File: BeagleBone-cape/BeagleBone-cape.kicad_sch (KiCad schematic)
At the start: 92 parts, among them IC2 TCAN3413DDFR, IC3 BMP390, IC4 BMM350, J1 Servo 0, J10 MotorR, J11 CAN, J12 24V, J13 MAVLink, J2 Servo 1, J3 Servo 2, J4 Servo 3, J5 LEDL, J6 LEDR, J7 MAG_I2C_TP, J8 Air Speed Sensor, J9 MotorL, P8 BeagleBone_Black_Header, P9 BeagleBone_Black_Header, Q2 Q_NMOS_GSD, SW1 SW_DIP_x02, U1 CAT24C256, U2 BHI360, U3 DS1307ZN+, Y1 32.768kHz

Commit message: Add i2c logic level translator
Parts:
- added C19: 100n, Capacitor_SMD:C_0603_1608Metric_Pad1.08x0.95mm_HandSolder, symbol Device:C_Small
- added C20, C21: 1u, Capacitor_SMD:C_0603_1608Metric_Pad1.08x0.95mm_HandSolder, symbol Device:C_Small
- added R25, R26: 4k7, Resistor_SMD:R_0603_1608Metric_Pad0.98x0.95mm_HandSolder, symbol Device:R_Small
- added R27: 200k, Resistor_SMD:R_0603_1608Metric_Pad0.98x0.95mm_HandSolder, symbol Device:R_Small
- added U4: TLV75518PDBV, Package_TO_SOT_SMD:SOT-23-5, symbol Regulator_Linear:TLV75518PDBV
- added U5: PCA9306DCUR, Package_SO:VSSOP-8_2.3x2mm_P0.5mm, symbol Interface:PCA9306DC
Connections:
- net +1V8: now also C21.1, U4.5 (OUT), U5.2 (VREF1); no longer P9.32 (Pin_32)
- net +3V3: now also R22.1, R23.1, C20.1, R25.1, R26.1, R27.1, U4.1 (IN), U4.3 (EN)
- net +5V: no longer R22.1, R23.1
- net GND: now also C19.2, C20.2, C21.2, U4.2 (GND), U5.1 (GND)
- net I2C1.SCL: now also U5.3 (SCL1); no longer P9.17 (Pin_17)
- net I2C1.SDA: now also U5.4 (SDA1); no longer P9.18 (Pin_18)
- net I2C_SCL_MAG: now also IC4.A3 (SCK), TP18.1; no longer IC4.A2 (SDA), TP17.1
- net I2C_SDA_MAG: now also IC4.A2 (SDA), TP17.1; no longer IC4.A3 (SCK), TP18.1
- new net I2C1_3V3.SCL: P9.17 (Pin_17), R25.2, U5.6 (SCL2)
- new net I2C1_3V3.SDA: P9.18 (Pin_18), R26.2, U5.5 (SDA2)
- new net I2C1_EN: C19.1, R27.2, U5.7 (VREF2), U5.8 (EN)
- no-connect marks 11 -> 13

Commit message: Update BeagleBone cape schematic/PCB, drop tracked KiCad backups
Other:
- moved on the sheet: BT1, BZ1, C1, C17, C18, C19, C2, C20, C21, C29, C3, C30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

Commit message: BeagleBone cape: add SN74LVC1T45 level shifters for BHI360 INT/RESET
BHI360 is a 1.8 V device (VDDIO max 1.89 V, abs max VDDIO+0.3 V), while
the AM335x P9 header is 3.3 V LVCMOS. Route INT (U2.4 -> P9.14) through
U7 (A->B, DIR=+1V8) and RESETN (P9.16 -> U2.17) through U8 (B->A,
DIR=GND). R28 10k holds RESET deasserted on the 3.3 V side while the pin
is undriven; C40-C43 decouple both sides.

PCB not yet updated from schematic; new parts still need placement and
routing. Some new parts sit off the 1.27 mm grid.
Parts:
- removed J7: MAG_I2C_TP, Connector_Wire:SolderWire-0.1sqmm_1x02_P3.6mm_D0.4mm_OD1mm, symbol Connector_Generic:Conn_01x02
- added C40, C41, C42, C43: 100n, Capacitor_SMD:C_0603_1608Metric_Pad1.08x0.95mm_HandSolder, symbol Device:C_Small
- added R28: 10k, Resistor_SMD:R_0603_1608Metric_Pad0.98x0.95mm_HandSolder, symbol Device:R_Small
- added U7, U8: SN74LVC1T45DBVR, Package_TO_SOT_SMD:SOT-23-6, symbol Logic_LevelTranslator:SN74LVC1T45DBV
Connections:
- net +1V8: now also C40.1, C42.1, U7.1 (VCCA), U7.5 (DIR), U8.1 (VCCA)
- net +3V3: now also C41.1, C43.1, R28.1, U7.6 (VCCB), U8.6 (VCCB)
- net BHI360_INT: now also U7.3 (A); no longer P9.14 (Pin_14)
- net BHI360_RESET: now also U8.3 (A); no longer P9.16 (Pin_16)
- net GND: now also C40.2, C41.2, C42.2, C43.2, U7.2 (GND), U8.2 (GND), U8.5 (DIR)
- new net BHI360_INT_3V3: P9.14 (Pin_14), U7.4 (B)
- new net BHI360_RESET_3V3: P9.16 (Pin_16), R28.2, U8.4 (B)
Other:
- moved on the sheet: R25, R26

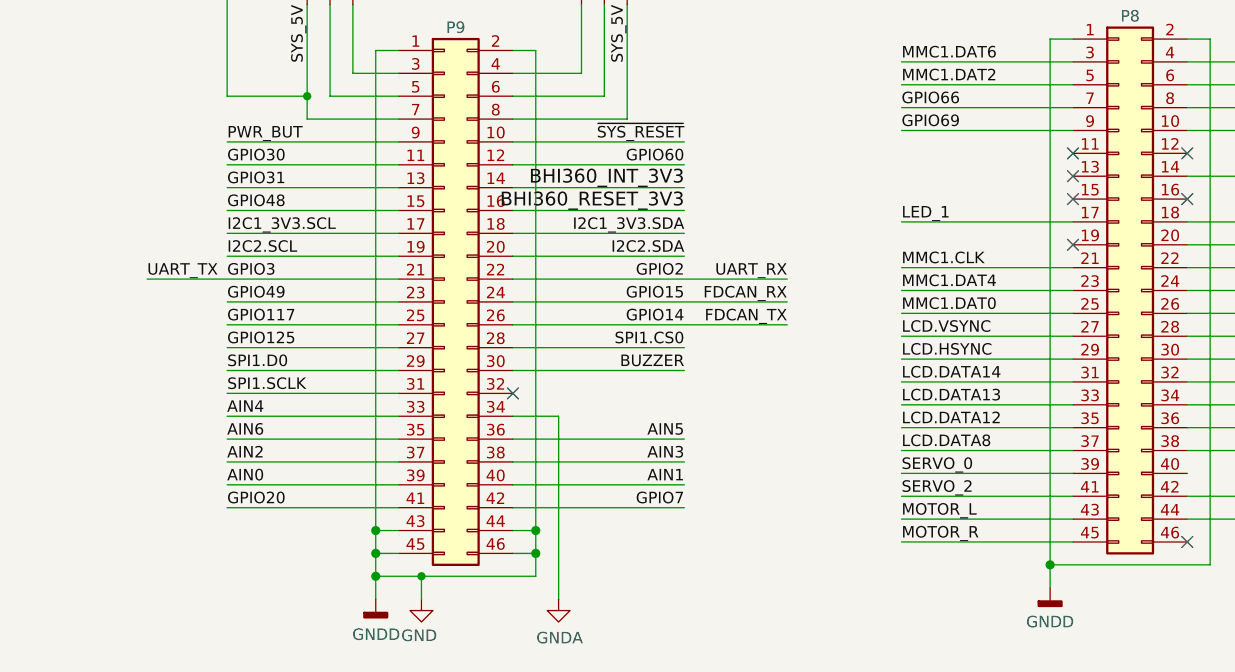
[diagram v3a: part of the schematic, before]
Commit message: BeagleBone cape: PCB/schematic updates, cape issues list, docs
- Update BeagleBone-cape KiCad schematic and PCB; add BHI360/BMP390 footprint updates
- Add ISSUES.md: cape design review findings (BHI360 1.8V/3.3V level shifting, etc.)
- Ignore .kicad-mcp/ local state
- Update docs/ROADMAP.md and docs/prus.md (PRU1 servo/ESC PWM design); README link
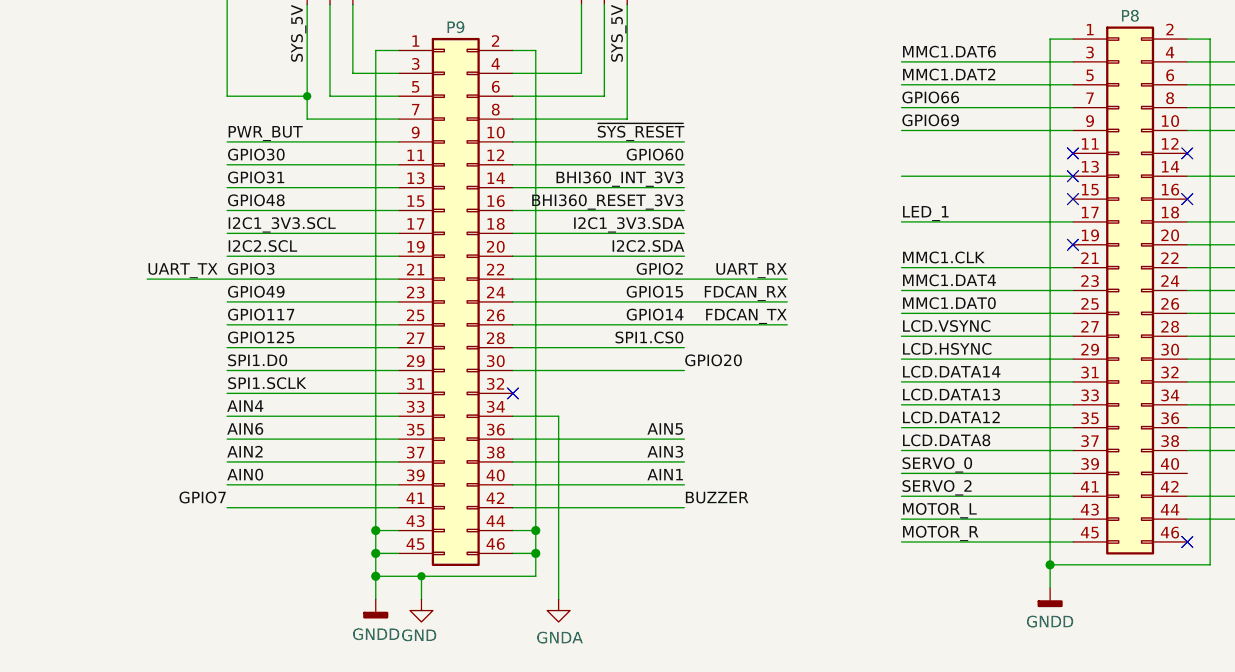
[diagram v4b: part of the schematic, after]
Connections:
- net BUZZER: now also P9.42 (Pin_42); no longer P9.30 (Pin_30)
- net GPIO20: now also P9.30 (Pin_30); no longer P9.41 (Pin_41)
- net GPIO7: now also P9.41 (Pin_41); no longer P9.42 (Pin_42)
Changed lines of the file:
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@@
 	)
 	(no_connect
+		(at 381 166.37)
+	)
+	(no_connect
 		(at 381 163.83)
 	)
@@
 	)
 	(no_connect
-		(at 381 166.37)
-	)
-	(no_connect
 		(at 134.62 76.2)
 	)
@@
 	(wire
 		(pts
+			(xy 361.95 166.37) (xy 381 166.37)
+		)
+		(stroke
+			(width 0)
+			(type default)
+		)
+	)
+	(wire
+		(pts
 			(xy 96.52 78.74) (xy 99.06 78.74)
 		)
@@
 		(effects
 			(font
-				(size 1.524 1.524)
+				(size 1.27 1.27)
 			)
 			(justify right bottom)
@@
 		)
 	)
+	(label "BUZZER"
+		(at 337.82 203.2 180)
+		(effects
+			(font
+				(size 1.27 1.27)
+			)
+			(justify left bottom)
+		)
+	)
 	(label "I2C2.SDA"
 		(at 325.12 69.85 0)
@@
 	)
 	(label "GPIO7"
-		(at 337.82 203.2 180)
+		(at 287.02 203.2 0)
 		(effects
 			(font
@@
 	)
 	(label "GPIO20"
-		(at 287.02 203.2 0)
+		(at 337.82 187.96 180)
 		(effects
 			(font
@@
 		)
 	)
-	(label "BUZZER"
-		(at 337.82 187.96 180)
-		(effects
-			(font
-				(size 1.27 1.27)
-			)
-			(justify right bottom)
-		)
-	)
 	(label "AIN0"
 		(at 287.02 200.66 0)
@@
 		(effects
 			(font
-				(size 1.524 1.524)
+				(size 1.27 1.27)
 			)
 			(justify right bottom)

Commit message: Cape: replace BHI360/BMM350 with LSM6DSV16X (SPI1) + IIS2MDC (I2C1)
- Remove BHI360, BMM350 and the 1.8 V domain (TLV75518, PCA9306, SN74LVC1T45 x2)
- Add LSM6DSV16X on SPI1 (P9.28-31), INT1/INT2 on P9.14/P9.16
- Add IIS2MDC on I2C1 (0x1E), DRDY on P9.15; BMP390 moved to 3.3 V on I2C1
- Move LED1 feed from P9.30 to P9.23 (P9.30 is now SPI1 D1)
- PCB: drop removed footprints and orphaned copper; new parts staged, not routed
- ISSUES.md: full cape review (issues 21-38); FUNCTIONS.md hardware mapping
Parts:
- removed C19, C4, C40, C41, C42, C43, C5, C6, C7: 100n, Capacitor_SMD:C_0603_1608Metric_Pad1.08x0.95mm_HandSolder, symbol Device:C_Small
- removed C20, C21, C3: 1u, Capacitor_SMD:C_0603_1608Metric_Pad1.08x0.95mm_HandSolder, symbol Device:C_Small
- removed C33: 220n, Capacitor_SMD:C_0603_1608Metric_Pad1.08x0.95mm_HandSolder, symbol Device:C_Small
- removed C39: 2u2F, Capacitor_SMD:C_0603_1608Metric_Pad1.08x0.95mm_HandSolder, symbol Device:C_Small
- removed D4: Blue, Diode_SMD:D_0603_1608Metric, symbol Device:LED_Small
- removed IC4: BMM350, symbol Cape_lib:BMM350
- removed R14, R28: 10k, Resistor_SMD:R_0603_1608Metric_Pad0.98x0.95mm_HandSolder, symbol Device:R_Small
- removed R15: 100, Resistor_SMD:R_0603_1608Metric_Pad0.98x0.95mm_HandSolder, symbol Device:R_Small
- removed R16, R17, R20, R21: 4k7, Resistor_SMD:R_0603_1608Metric_Pad0.98x0.95mm_HandSolder, symbol Device:R_Small
- removed R27: 200k, Resistor_SMD:R_0603_1608Metric_Pad0.98x0.95mm_HandSolder, symbol Device:R_Small
- removed TP17, TP18, TP22: TestPoint, TestPoint:TestPoint_Pad_D1.0mm, symbol Connector:TestPoint
- removed U2: BHI360, symbol Cape_lib:BHI360
- removed U4: TLV75518PDBV, Package_TO_SOT_SMD:SOT-23-5, symbol Regulator_Linear:TLV75518PDBV
- removed U5: PCA9306DCUR, Package_SO:VSSOP-8_2.3x2mm_P0.5mm, symbol Interface:PCA9306DC
- removed U7, U8: SN74LVC1T45DBVR, Package_TO_SOT_SMD:SOT-23-6, symbol Logic_LevelTranslator:SN74LVC1T45DBV
- added C44, C45, C46, C47: 100n, Capacitor_SMD:C_0603_1608Metric_Pad1.08x0.95mm_HandSolder, symbol Device:C_Small
- added C48: 220n, Capacitor_SMD:C_0603_1608Metric_Pad1.08x0.95mm_HandSolder, symbol Device:C_Small
- added U10: IIS2MDC, Package_LGA:LGA-12_2x2mm_P0.5mm, symbol Cape_lib:IIS2MDC
- added U9: LSM6DSV16X, Package_LGA:LGA-14_3x2.5mm_P0.5mm_LayoutBorder3x4y, symbol Cape_lib:LSM6DSV16X
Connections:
- net +1V8 is gone; now on net +3V3: C1.1, C2.1, IC3.1 (VDDIO), IC3.10 (VDD), IC3.6 (CSB), R8.1, R9.1
- net BHI360_INT_3V3 is gone; now on net IMU_INT1: P9.14 (Pin_14)
- net BHI360_RESET_3V3 is gone; now on net IMU_INT2: P9.16 (Pin_16)
- net I2C1_3V3.SCL is gone; now on net I2C1.SCL: P9.17 (Pin_17), R25.2
- net I2C1_3V3.SDA is gone; now on net I2C1.SDA: P9.18 (Pin_18), R26.2
- net JTAG_DIO is gone; now on net MAG_DRDY: TP16.1
- net +3V3: now also C44.1, C45.1, C46.1, C47.1, U10.10 (Vdd_IO), U10.3 (~{CS}), U10.9 (Vdd), U9.5 (VDDIO), U9.8 (VDD)
- net GND: now also C44.2, C45.2, C46.2, C47.2, C48.2, U10.6 (GND), U10.8 (GND), U9.2 (SDx), U9.3 (SCx), U9.6 (GND), U9.7 (GND)
- net GPIO49: now also R11.2, TP33.1
- net I2C1.SCL: now also U10.1 (SCL/SPC)
- net I2C1.SDA: now also U10.4 (SDA/SDI/SDO)
- net SPI1.CS0: now also U9.12 (CS)
- net SPI1.D0: now also U9.1 (SDO/SA0)
- net SPI1.SCLK: now also U9.13 (SCL)
- net BHI360_INT renamed IMU_INT1
- net IMU_INT1: now also U9.4 (INT1)
- net BHI360_RESET renamed IMU_INT2
- net IMU_INT2: now also U9.9 (INT2)
- removed net GPIO20: P9.30 (Pin_30), R11.2, TP33.1
- net GPIO48 renamed MAG_DRDY
- net MAG_DRDY: now also U10.7 (DRDY)
- net INT renamed BARO_INT
- new net: C48.1, U10.5 (C1)
- new net SPI1.D1: P9.30 (Pin_30), U9.14 (SDA)
- no-connect marks 13 -> 10
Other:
- note added: "BMP390 - Barometer (I2C1, 0x76)"
- note added: "IIS2MDC - Magnetometer (I2C1, 0x1E)"
- note added: "LSM6DSV16X - 6DoF IMU (SPI1)"
- note removed: "BHI360 - 6DoF accelerometer and gyro"
- note removed: "BMM350 - Magnetometer"
- note removed: "BMP390 - Barometer"
- moved on the sheet: TP16, TP23, TP24

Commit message: Cape: finish IMU/baro schematic, PCB sync and cleanup
Schematic:
- remove cape EEPROM U1, SW1, TP1 (#4)
- PGOOD to P8.12 via 10k pull-up R27 (#10)
- PWR_FLAGs on root, VBUS renamed SYS_5V, GPIO2/3 renamed UART_RX/TX (#6, #12, #33)
- VBIAS of A6983 to BUCK_OUT (#34)
- BMP390 symbol moved to Cape_lib, MPN fixed BMP388 -> BMP390 (#13)
- LSM6DSV16X/IIS2MDC: add C49 10 uF decoupling, fix C48 value/MPN (datasheet audit)

PCB:
- sync from schematic, place U9, U10, C44-C49, R27
- remove stray IMU-area +3V3/IMU_INT1 copper, old +3V3 In2 pour, dangling copper (#17, #18)
- design rules: outer track 0.10 mm, edge clearance 0.3 mm, zone clearance 0.2 mm (#37)

Routing is not done: 46 unconnected pads remain for manual routing.
DRC: 1 courtyard overlap (R27/R18), 7 pre-existing lib_footprint_mismatch warnings.
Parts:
- removed SW1: SW_DIP_x02, symbol Switch:SW_DIP_x02
- removed TP1: WP, symbol Connector:TestPoint
- removed U1: CAT24C256, symbol Memory_EEPROM:CAT24C256
- added C49: 10u, Capacitor_SMD:C_0603_1608Metric_Pad1.08x0.95mm_HandSolder, symbol Device:C_Small
- added R27: 10k, Resistor_SMD:R_0603_1608Metric_Pad0.98x0.95mm_HandSolder, symbol Device:R_Small
- C48: Manufacturer_Name (none) -> HRE; Mouser Part Number 81-GRM155R61A224KE9J -> (none); Part number 220n-10V-X5R-10% -> 220n-50V-X7R-10%
- IC2: footprint (none) -> caplib:SOT65P280X110-8N
- IC3: footprint (none) -> caplib:BMP390; symbol sensor_fuser_symbol:BMP390 -> Cape_lib:BMP390; Manufacturer_Part_Number BMP388 -> BMP390
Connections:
- net +3V3: now also C49.1, R27.1
- net GND: now also C49.2
- net PGOOD: now reaches P8.12 (Pin_12)
- net PGOOD: now also R27.2
- net GPIO2 renamed UART_RX
- net GPIO3 renamed UART_TX
- net VBUS renamed SYS_5V
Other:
- sheet Power ports: added PGOOD; removed none
- company: (none) -> Skylark
- title: (none) -> Skylark BeagleBone Black cape

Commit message: Cape: add baro and IMU/mag schematic sheets, sync root/PCB/project files
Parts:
- removed C1, C2, C44, C45, C46, C47: 100n, Capacitor_SMD:C_0603_1608Metric_Pad1.08x0.95mm_HandSolder, symbol Device:C_Small
- removed C48: 220n, Capacitor_SMD:C_0603_1608Metric_Pad1.08x0.95mm_HandSolder, symbol Device:C_Small
- removed C49: 10u, Capacitor_SMD:C_0603_1608Metric_Pad1.08x0.95mm_HandSolder, symbol Device:C_Small
- removed IC3: BMP390, caplib:BMP390, symbol Cape_lib:BMP390
- removed R8, R9: 4k7, Resistor_SMD:R_0603_1608Metric_Pad0.98x0.95mm_HandSolder, symbol Device:R_Small
- removed TP16, TP19, TP20, TP21, TP23, TP24: TestPoint, TestPoint:TestPoint_Pad_D1.0mm, symbol Connector:TestPoint
- removed U10: IIS2MDC, Package_LGA:LGA-12_2x2mm_P0.5mm, symbol Cape_lib:IIS2MDC
- removed U9: LSM6DSV16X, Package_LGA:LGA-14_3x2.5mm_P0.5mm_LayoutBorder3x4y, symbol Cape_lib:LSM6DSV16X
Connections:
- net GPIO125 renamed IMU2_CS
- net GPIO60 renamed IMU2_INT1
- no-connect marks 10 -> 8
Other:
- added sheet Barometer (baro.kicad_sch)
- added sheet IMU + MAG (imu_mag.kicad_sch)
- note removed: "BMP390 - Barometer (I2C1, 0x76)"
- note removed: "IIS2MDC - Magnetometer (I2C1, 0x1E)"
- note removed: "LSM6DSV16X - 6DoF IMU (SPI1)"
- moved on the sheet: J4, P8, P9, TP32, TP33, TP34, TP6
